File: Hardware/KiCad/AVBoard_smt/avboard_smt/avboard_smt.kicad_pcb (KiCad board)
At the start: 4 copper layers, 177 x 152.1 mm, 111 parts, among them IC2_AUD0 7432N, IC36 4040N, IC37 7430N, IC39 7400N, IC40 4040N, IC41 7400N, IC43 7400N, IC44 7486N, IC45 7400N, IC46 74257N, IC47 74257N, IC48 74564N, IC4_AUD0 7400N, IC53 7404N, IC6_AUD0 7474N, IC7_AUD0 LM358N, J1 5V, J2 VID_TO_MOBO, U1 W65C02SP, U2 THS7374

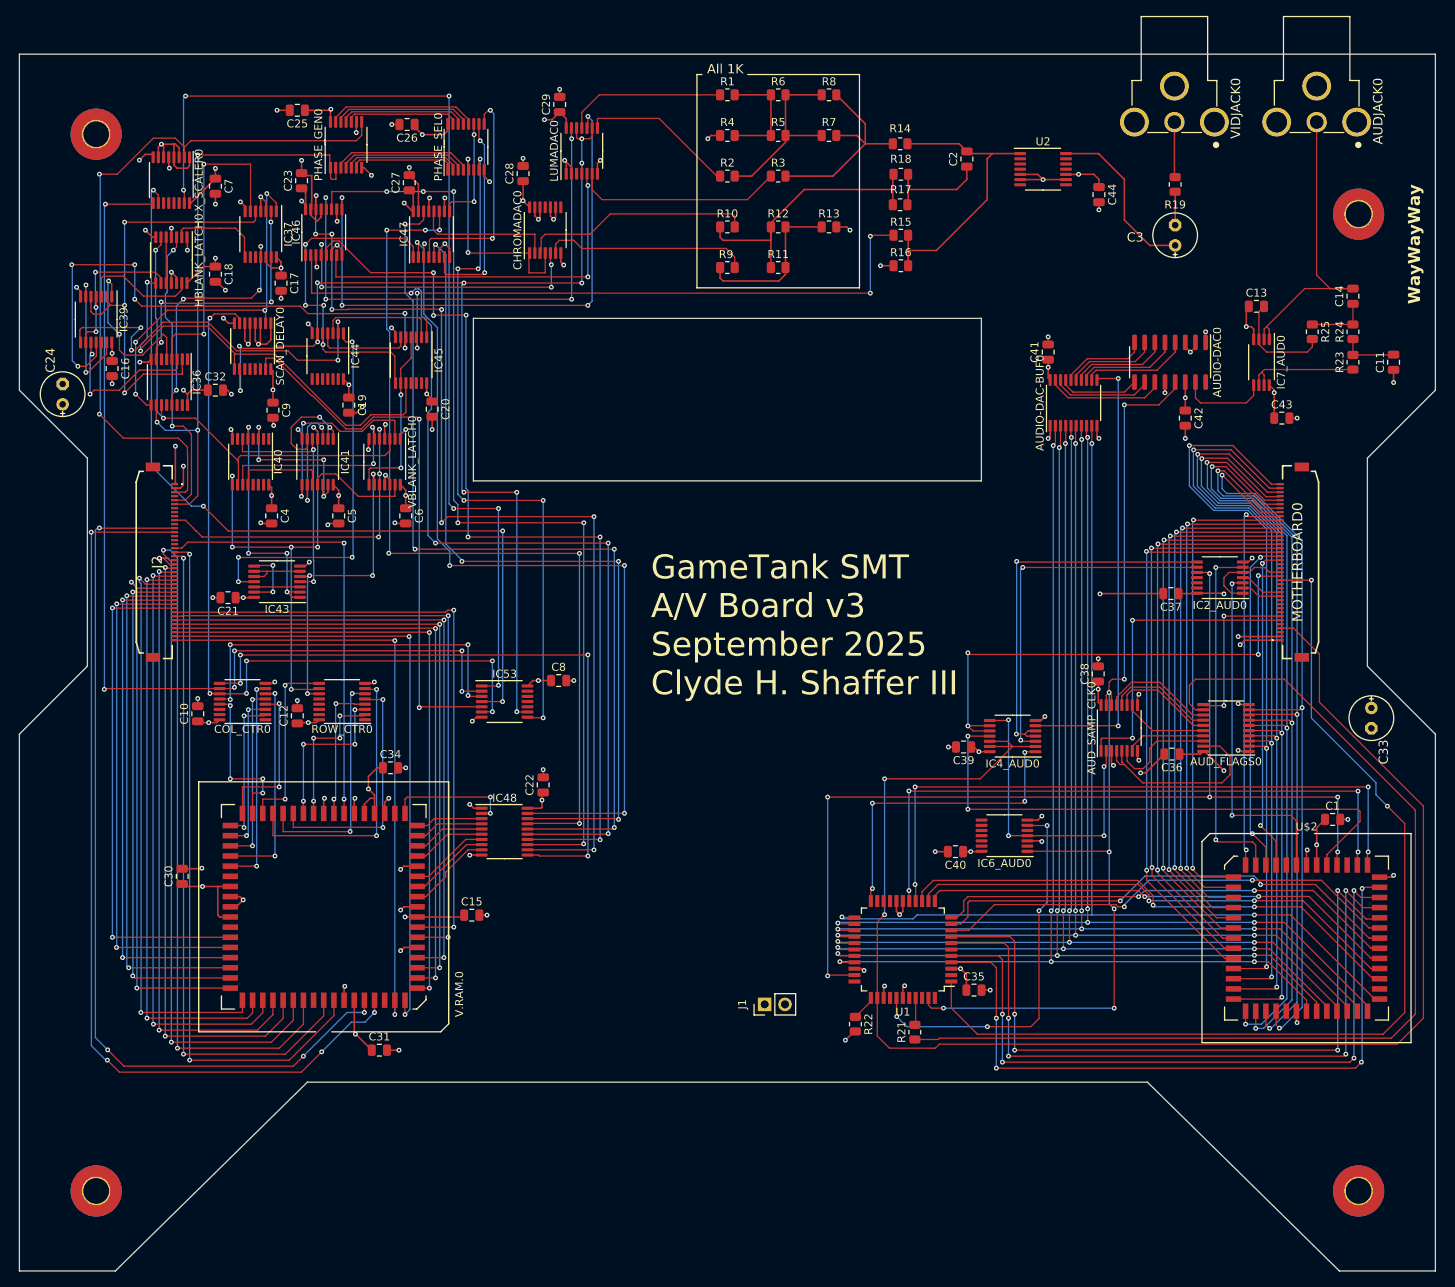
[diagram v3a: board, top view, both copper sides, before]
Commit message: replace dual ported frame buffer with mirrored single ported rams
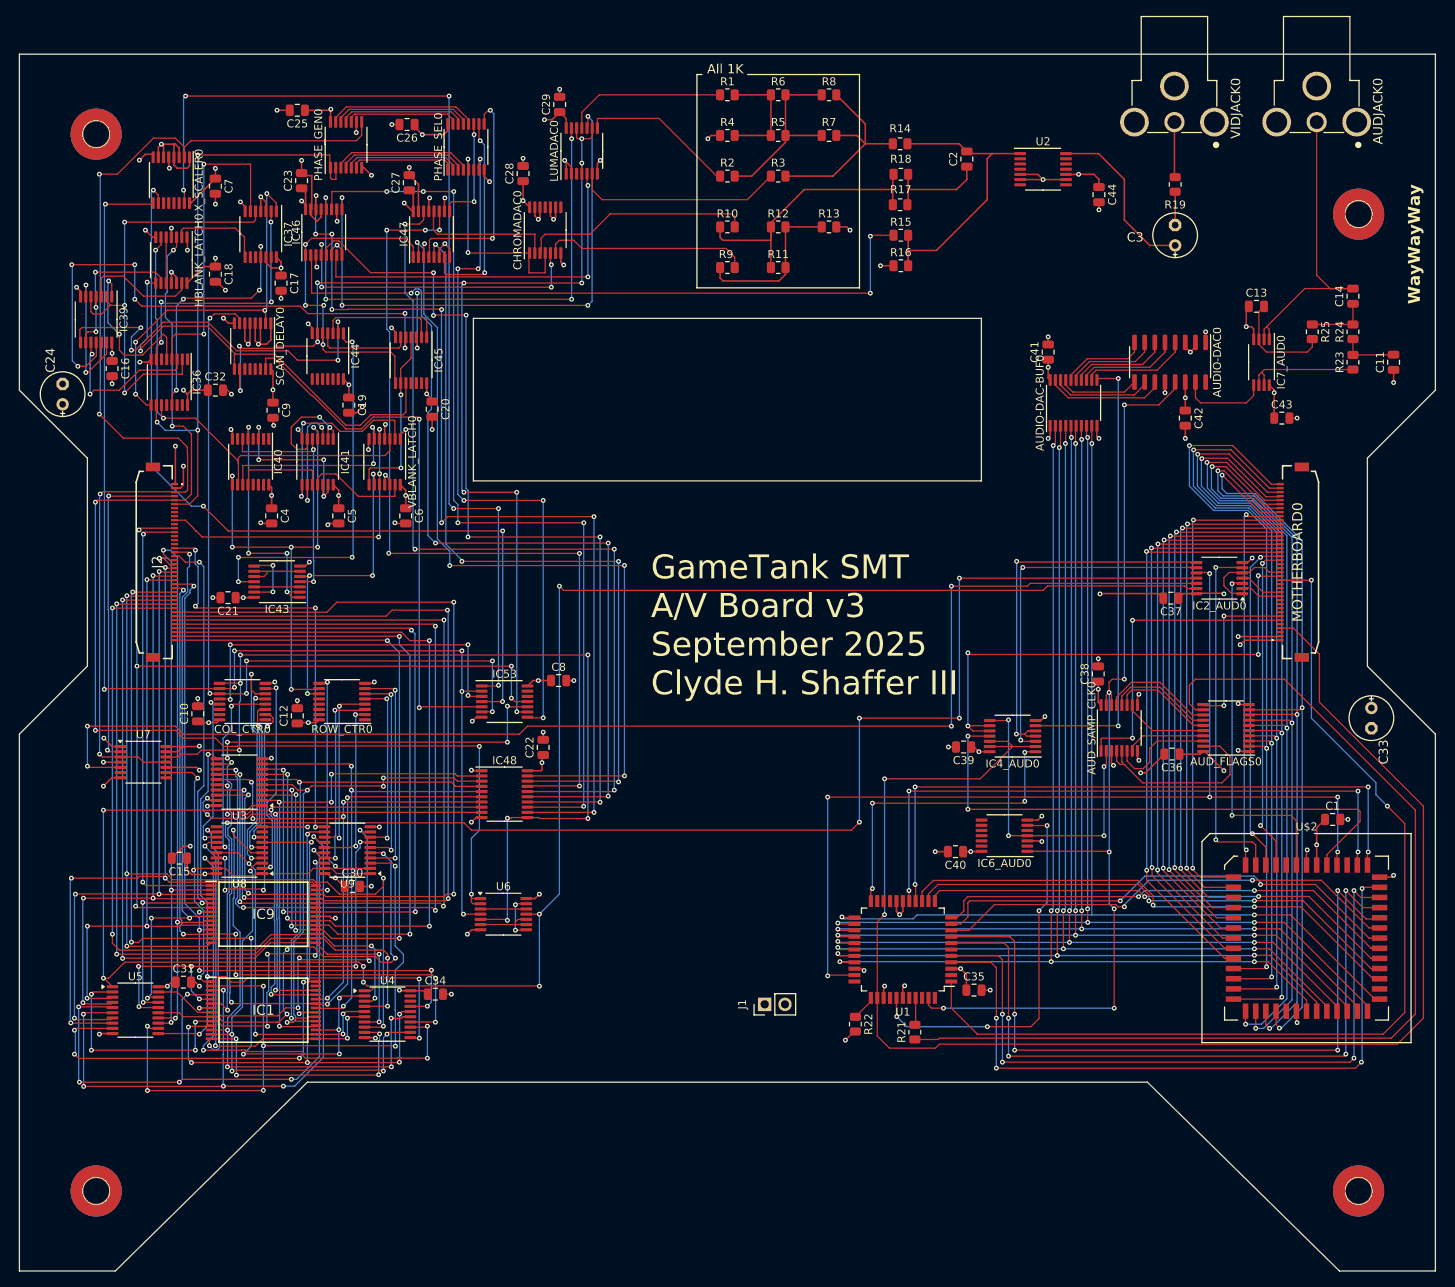
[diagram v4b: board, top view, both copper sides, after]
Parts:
- removed V.RAM.0: PDPRAM_32K_V2, Package_LCC:PLCC-68_SMD-Socket
- added IC1: AS7C256A-10TIN, SamacSys_Parts:SOP55P1340X120-28N, F.Cu at (90.5, 161.0)
- added IC9: AS7C256A-10TIN, SamacSys_Parts:SOP55P1340X120-28N, F.Cu at (90.5, 149.0)
- added U3: 74AHC373, Package_SO:TSSOP-20_4.4x6.5mm_P0.65mm, F.Cu at (87.5, 132.5)
- added U4: 74AHC373, Package_SO:TSSOP-20_4.4x6.5mm_P0.65mm, F.Cu at (106.0, 161.5)
- added U5: 74AHC373, Package_SO:TSSOP-20_4.4x6.5mm_P0.65mm, F.Cu at (74.5, 161.0)
- added U6: 74AC00, Package_SO:TSSOP-14_4.4x5mm_P0.65mm, F.Cu at (120.5, 149.0)
- added U7: 74VHC74, Package_SO:TSSOP-14_4.4x5mm_P0.65mm, F.Cu at (75.5, 130.0)
- added U8: 74HC244, Package_SO:TSSOP-20_4.4x6.5mm_P0.65mm, F.Cu at (87.5, 141.0)
- added U9: 74HC244, Package_SO:TSSOP-20_4.4x6.5mm_P0.65mm, F.Cu at (101.0, 141.0)
- moved C15 37.2 mm to (80.0, 142.0), turned to 180 degrees
- moved C34 28.8 mm to (112.0, 159.0)
- moved C31 25.9 mm to (80.5, 157.5)
- moved C30 21.3 mm to (101.6, 145.5), turned to 0 degrees
- moved C22 4.68 mm to (125.5, 128.2)
- moved IC48 4.68 mm to (120.7, 134.0)
- moved C37 0.57 mm to (203.9, 109.5)
- moved IC2_AUD0 0.09 mm to (210.0, 107.0)
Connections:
- net Net-(COL_CTR0A-Q1) renamed /Composite Video Generator/PIXLATCH
- COL_CTR0 pad 13: Net-(COL_CTR0A-Q8) -> PAX6
- COL_CTR0 pad 2: Net-(COL_CTR0A-Q6) -> PAX4
- COL_CTR0 pad 3: Net-(COL_CTR0A-Q5) -> PAX3
- COL_CTR0 pad 4: Net-(COL_CTR0A-Q7) -> PAX5
- COL_CTR0 pad 5: Net-(COL_CTR0A-Q4) -> PAX2
- COL_CTR0 pad 6: Net-(COL_CTR0A-Q3) -> PAX1
- COL_CTR0 pad 7: Net-(COL_CTR0A-Q2) -> PAX0
- IC2_AUD0 pad 11: unconnected-(IC2_AUD0D-O-Pad11) -> /Composite Video Generator/~{MirrorWE}
- IC2_AUD0 pad 12: unconnected-(IC2_AUD0D-I0-Pad12) -> /Composite Video Generator/LAG14
- IC2_AUD0 pad 13: unconnected-(IC2_AUD0D-I1-Pad13) -> /Composite Video Generator/~{MirrorLoad}
- IC48 pad 2: /Composite Video Generator/P7 -> P7
- IC48 pad 3: /Composite Video Generator/P6 -> P6
- IC48 pad 4: /Composite Video Generator/P5 -> P5
- IC48 pad 5: /Composite Video Generator/P4 -> P4
- IC48 pad 6: /Composite Video Generator/P3 -> P3
- IC48 pad 7: /Composite Video Generator/P2 -> P2
- IC48 pad 8: /Composite Video Generator/P1 -> P1
- IC48 pad 9: /Composite Video Generator/P0 -> P0
- IC53 pad 10: (no net) -> /Composite Video Generator/VWE
- IC53 pad 11: (no net) -> /Composite Video Generator/~{VWE}
- J2 pad 17: /Composite Video Generator/VIDPAGE -> VIDPAGE
- J2 pad 18: /Composite Video Generator/VA14 -> VA14
- J2 pad 19: /Composite Video Generator/VA13 -> VA13
- J2 pad 20: /Composite Video Generator/VA12 -> VA12
- J2 pad 21: /Composite Video Generator/VA11 -> VA11
- J2 pad 22: /Composite Video Generator/VA10 -> VA10
- J2 pad 23: /Composite Video Generator/VA9 -> VA9
- J2 pad 24: /Composite Video Generator/VA8 -> VA8
- J2 pad 25: /Composite Video Generator/VA7 -> VA7
- J2 pad 26: /Composite Video Generator/VA6 -> VA6
- J2 pad 27: /Composite Video Generator/VA5 -> VA5
- J2 pad 28: /Composite Video Generator/VA4 -> VA4
- J2 pad 29: /Composite Video Generator/VA3 -> VA3
- J2 pad 30: /Composite Video Generator/VA2 -> VA2
- J2 pad 31: /Composite Video Generator/VA1 -> VA1
- J2 pad 32: /Composite Video Generator/VA0 -> VA0
- J2 pad 33: /Composite Video Generator/VD7 -> VD7
- J2 pad 34: /Composite Video Generator/VD6 -> VD6
- J2 pad 35: /Composite Video Generator/VD5 -> VD5
- J2 pad 36: /Composite Video Generator/VD4 -> VD4
- J2 pad 37: /Composite Video Generator/VD3 -> VD3
- J2 pad 38: /Composite Video Generator/VD2 -> VD2
- J2 pad 39: /Composite Video Generator/VD1 -> VD1
- J2 pad 40: /Composite Video Generator/VD0 -> VD0
- ROW_CTR0 pad 2: Net-(ROW_CTR0A-Q6) -> PAY5
- ROW_CTR0 pad 3: Net-(ROW_CTR0A-Q5) -> PAY4
- ROW_CTR0 pad 4: Net-(ROW_CTR0A-Q7) -> PAY6
- ROW_CTR0 pad 5: Net-(ROW_CTR0A-Q4) -> PAY3
- ROW_CTR0 pad 6: Net-(ROW_CTR0A-Q3) -> PAY2
- ROW_CTR0 pad 7: Net-(ROW_CTR0A-Q2) -> PAY1
- ROW_CTR0 pad 9: Net-(ROW_CTR0A-Q1) -> PAY0
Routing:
- net /Composite Video Generator/~{MirrorLoad}: track 0.00 -> 235.0 mm, vias 0 -> 7
- net /Composite Video Generator/~{MirrorWE}: track 0.00 -> 178.7 mm, vias 0 -> 6
- net /Composite Video Generator/LAG14: track 0.00 -> 166.3 mm, vias 0 -> 4
- net /Composite Video Generator/VWE: track 0.00 -> 123.6 mm, vias 0 -> 9
- net VA3: track 0.00 -> 115.9 mm, vias 0 -> 5
- net VD7: track 0.00 -> 114.6 mm, vias 0 -> 4
- net VD5: track 0.00 -> 114.1 mm, vias 0 -> 4
- net VD6: track 0.00 -> 113.4 mm, vias 0 -> 4
- net VD4: track 0.00 -> 113.0 mm, vias 0 -> 4
- net /Composite Video Generator/CLK7: track 37.3 -> 147.0 mm, vias 2 -> 6
- net VA4: track 0.00 -> 108.4 mm, vias 0 -> 6
- net VD2: track 0.00 -> 107.3 mm, vias 0 -> 4
- net VD3: track 0.00 -> 102.0 mm, vias 0 -> 4
- net VD1: track 0.00 -> 102.0 mm, vias 0 -> 4
- net VD0: track 0.00 -> 99.2 mm, vias 0 -> 4
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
